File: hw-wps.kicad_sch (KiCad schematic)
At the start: 8 parts, among them J1 GPIO, J2 Screw_Terminal_01x03, U2 ESP32DevKitv1

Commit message: Separate 3V3 nets, add i2c solder bridges & add capacitors to adc sensor
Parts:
- added C1, C2: C, symbol Device:C
- added JP1, JP2, JP3, JP4: SolderJumper_2_Bridged, symbol Jumper:SolderJumper_2_Bridged
- R3: value 1k -> 5k
- R4: value 2k -> 10k
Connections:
- net +3V3: no longer U2.1 (3V3)
- net +5V: now also C1.2
- net ADC_IN: now also C2.2
- net GND: now also C1.1, C2.1
- net GPIO2/SDA1: now also JP4.2 (B)
- net GPIO3/SCL1: now also JP2.2 (B)
- net SCL: now also JP1.1 (A), JP2.1 (A); no longer U2.14 (D22)
- net SDA: now also JP3.1 (A), JP4.1 (A); no longer U2.11 (D21)
- new net SCL_ESP32: JP1.2 (B), U2.14 (D22)
- new net SDA_ESP32: JP3.2 (B), U2.11 (D21)
- no-connect marks 47 -> 46
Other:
- note added: "I2C solder bridges"
- moved on the sheet: Brd1, J2

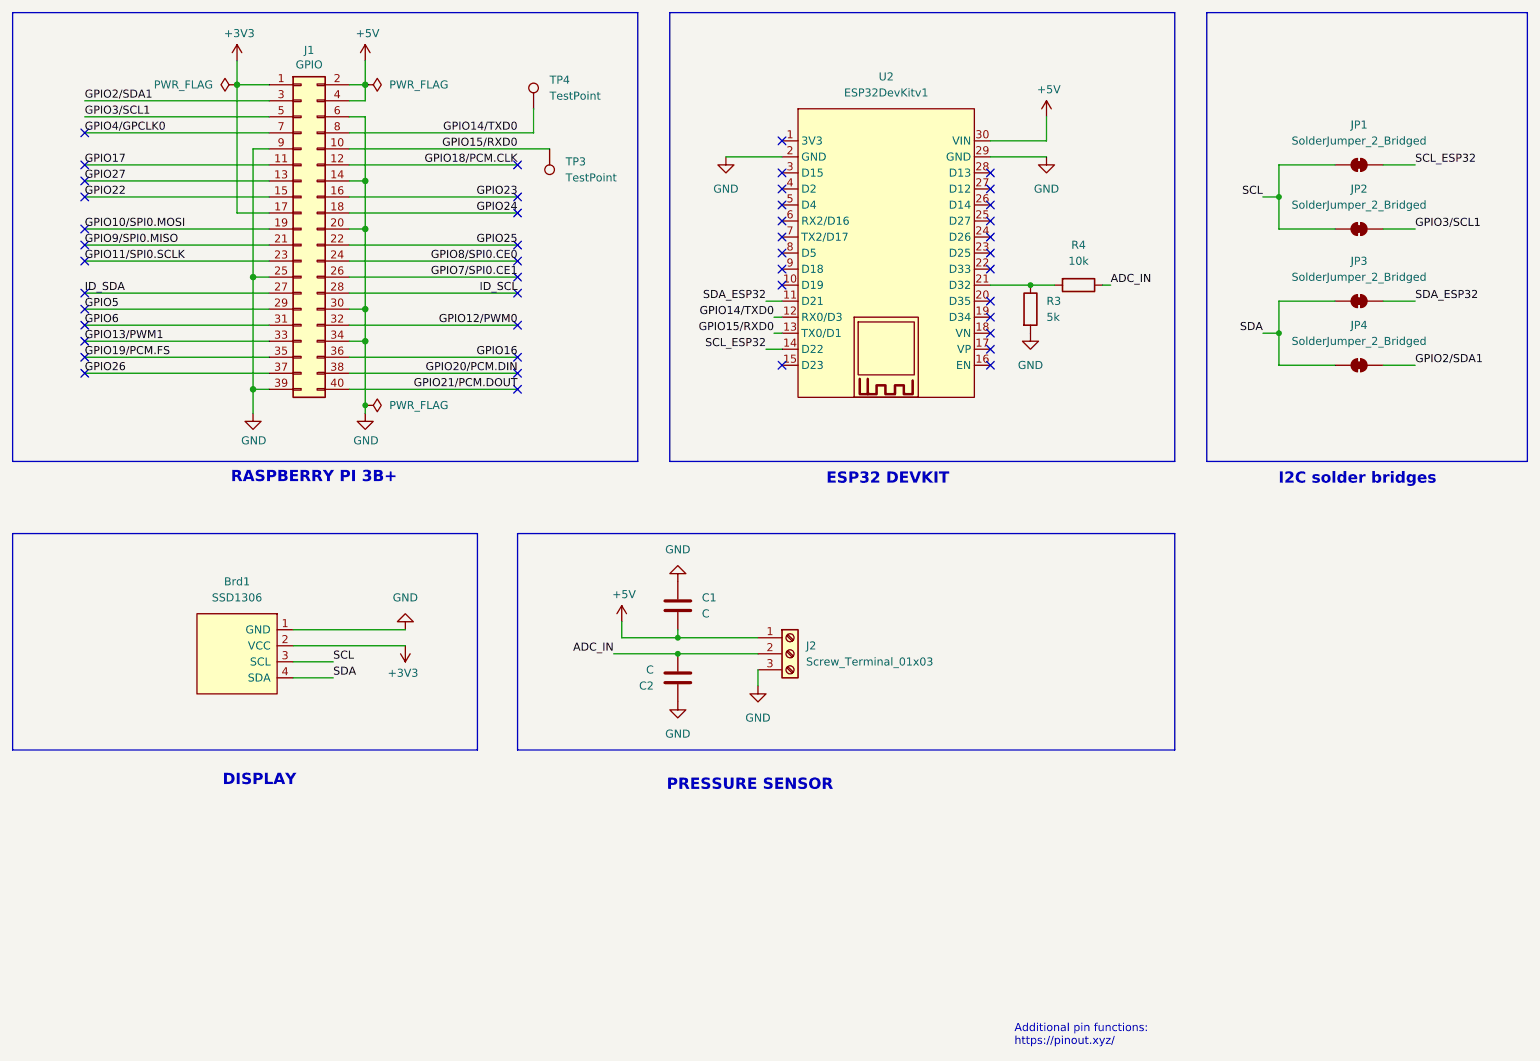
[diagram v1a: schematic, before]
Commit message: Update routing with previous changes
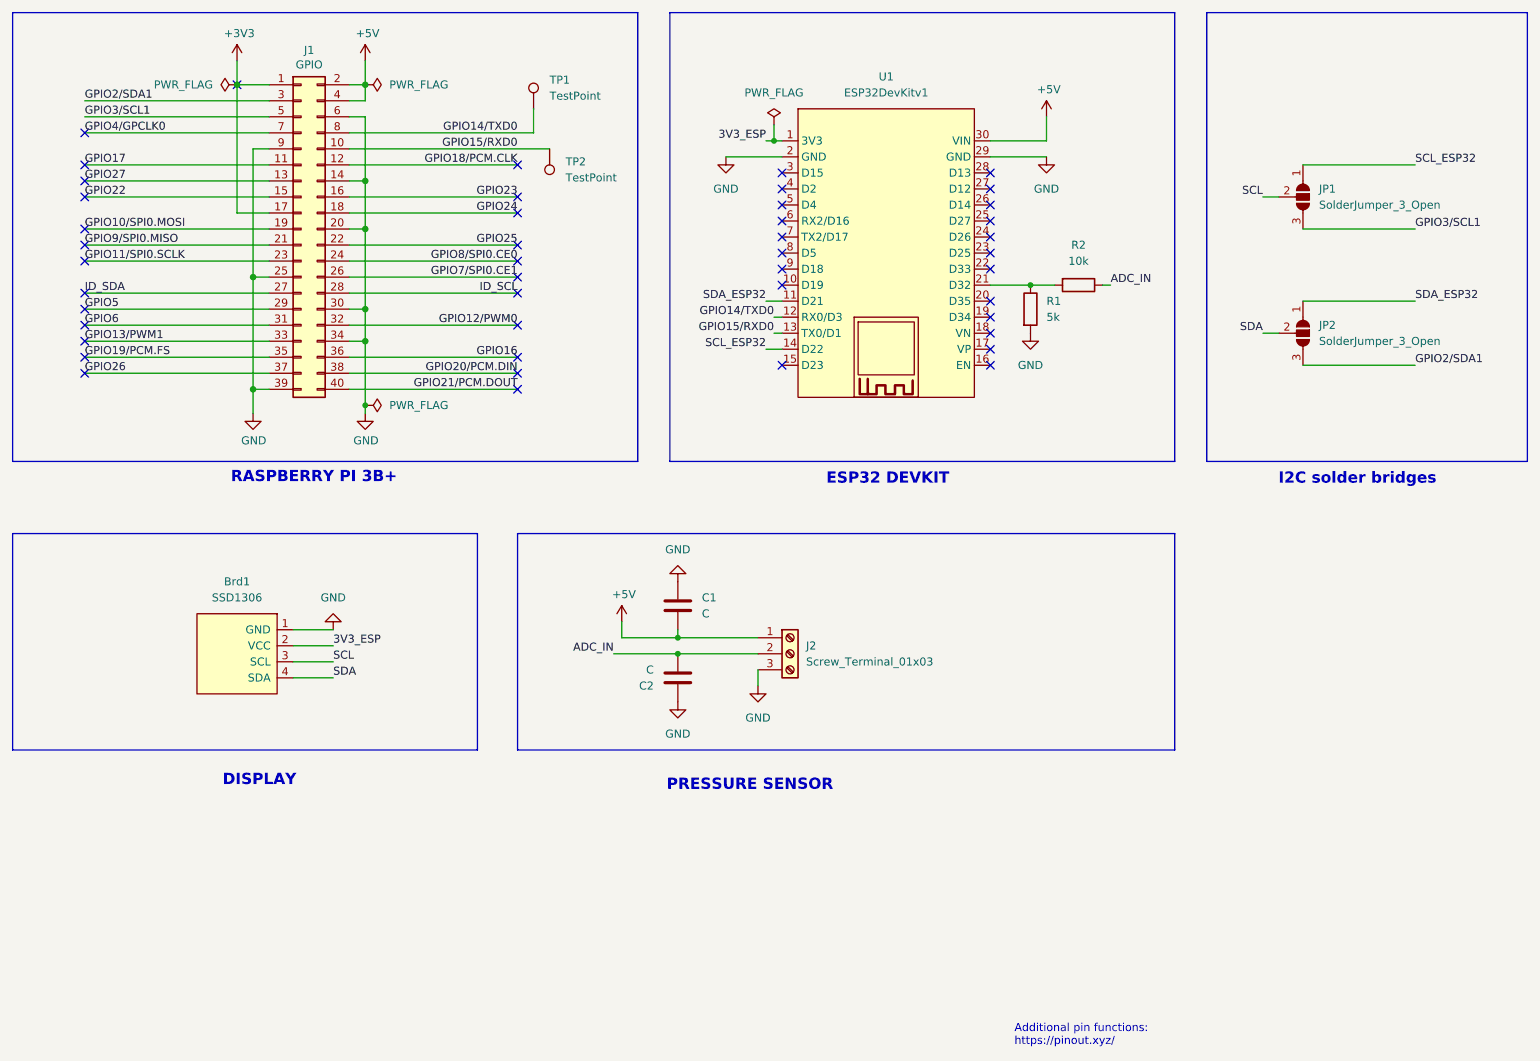
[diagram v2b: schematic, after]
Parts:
- removed JP1, JP2, JP3, JP4: SolderJumper_2_Bridged, symbol Jumper:SolderJumper_2_Bridged
- added JP1, JP2: SolderJumper_3_Open, Jumper:SolderJumper-3_P1.3mm_Open_RoundedPad1.0x1.5mm, symbol Jumper:SolderJumper_3_Open
- C1, C2: footprint (none) -> Capacitor_THT:CP_Radial_D5.0mm_P2.50mm
- renumbered R3 to R1, R4 to R2, TP4 to TP1, TP3 to TP2, U2 to U1
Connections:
- net +3V3: no longer Brd1.2 (VCC)
- net GPIO2/SDA1: now also JP2.3 (B)
- net GPIO3/SCL1: now also JP1.3 (B)
- net SCL: now also JP1.2 (C)
- net SCL_ESP32: now also JP1.1 (A)
- net SDA: now also JP2.2 (C)
- net SDA_ESP32: now also JP2.1 (A)
- net 3V3_ESP: now reaches U1.1 (3V3)
- net 3V3_ESP: now also Brd1.2 (VCC)

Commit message: Release v0.2
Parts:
- removed J1: GPIO, Connector_PinSocket_2.54mm:PinSocket_2x20_P2.54mm_Vertical, symbol Connector_Generic:Conn_02x20_Odd_Even
- removed JP1, JP2: SolderJumper_3_Open, Jumper:SolderJumper-3_P1.3mm_Open_RoundedPad1.0x1.5mm, symbol Jumper:SolderJumper_3_Open
- added J1: Screw_Terminal_01x02, TerminalBlock:TerminalBlock_MaiXu_MX126-5.0-02P_1x02_P5.00mm, symbol Connector:Screw_Terminal_01x02
- added SD1: SD card reader, SD_card_I2C:SD_card_I2C, symbol SD_card_I2C:SD_card_I2C
- TP1, TP2: footprint TestPoint:TestPoint_Pad_D2.0mm -> TestPoint:TestPoint_Pad_1.5x1.5mm
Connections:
- net SCL_ESP32 is gone; now on net SCL: U1.14 (D22)
- net SDA_ESP32 is gone; now on net SDA: U1.11 (D21)
- net +5V: now also J1.1 (Pin_1), SD1.3 (+5)
- net GND: now also J1.2 (Pin_2), SD1.1 (GND), SD1.8 (GND)
- net MISO: now reaches U1.10 (D19)
- net MISO: now also SD1.7 (MISO)
- net MOSI: now reaches U1.15 (D23)
- net MOSI: now also SD1.5 (MOSI)
- net CS: now reaches U1.4 (D2)
- net CS: now also SD1.4 (CS)
- net SCK: now reaches U1.9 (D18)
- net SCK: now also SD1.6 (SCK)
- net GPIO14/TXD0: no longer names the net of TP1.1, U1.12 (RX0/D3)
- net GPIO15/RXD0: no longer names the net of TP2.1, U1.13 (TX0/D1)
- no-connect marks 46 -> 18
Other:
- note added: "POWER SUPPLY"
- note added: "Power alternatives: - USB type-C directly to ESP32. - 5VDC using external power supply. i.e. LM2596 for 9V-40V or 5VDC UPS."
- note added: "SD CARD"
- note removed: "I2C solder bridges"
- note removed: "RASPBERRY PI 3B+"
- moved on the sheet: R1, R2, U1
